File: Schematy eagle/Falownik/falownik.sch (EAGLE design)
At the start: 43 parts, among them IC1 A1382UA, IC2 A1382UA, IC3 A1382UA, IC4 A1382UA, IC5 A1382UA, IC6 A1382UA, IC7 A1382UA, IC8 A1382UA, IC9 A1382UA, Q1 VN88AF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

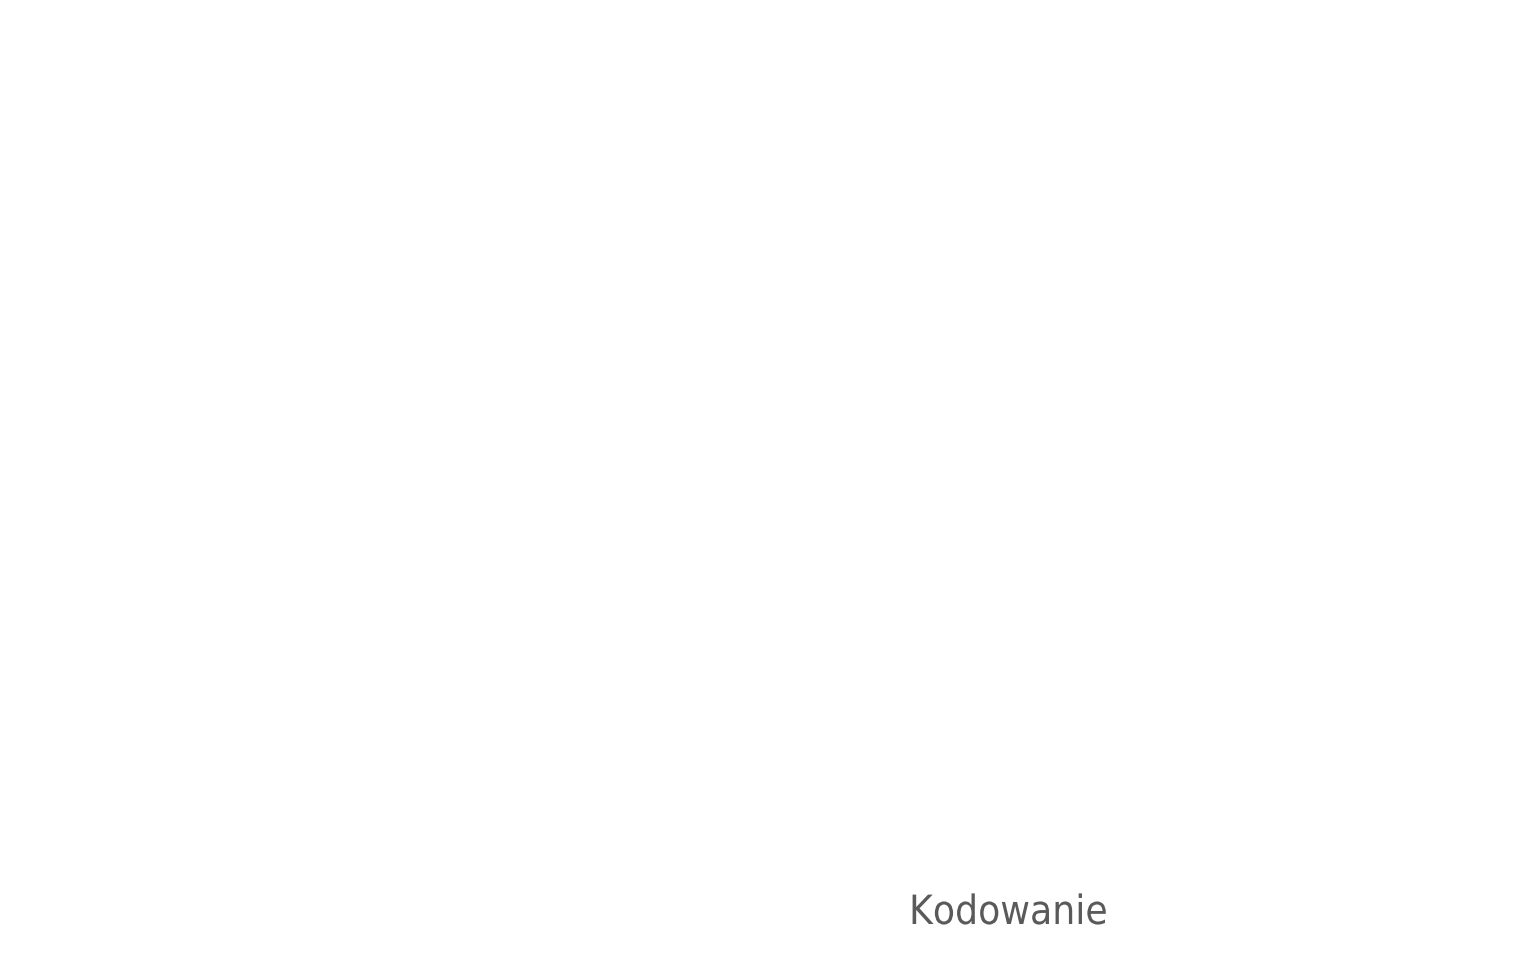
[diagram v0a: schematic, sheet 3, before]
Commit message: Dodanie kodowania
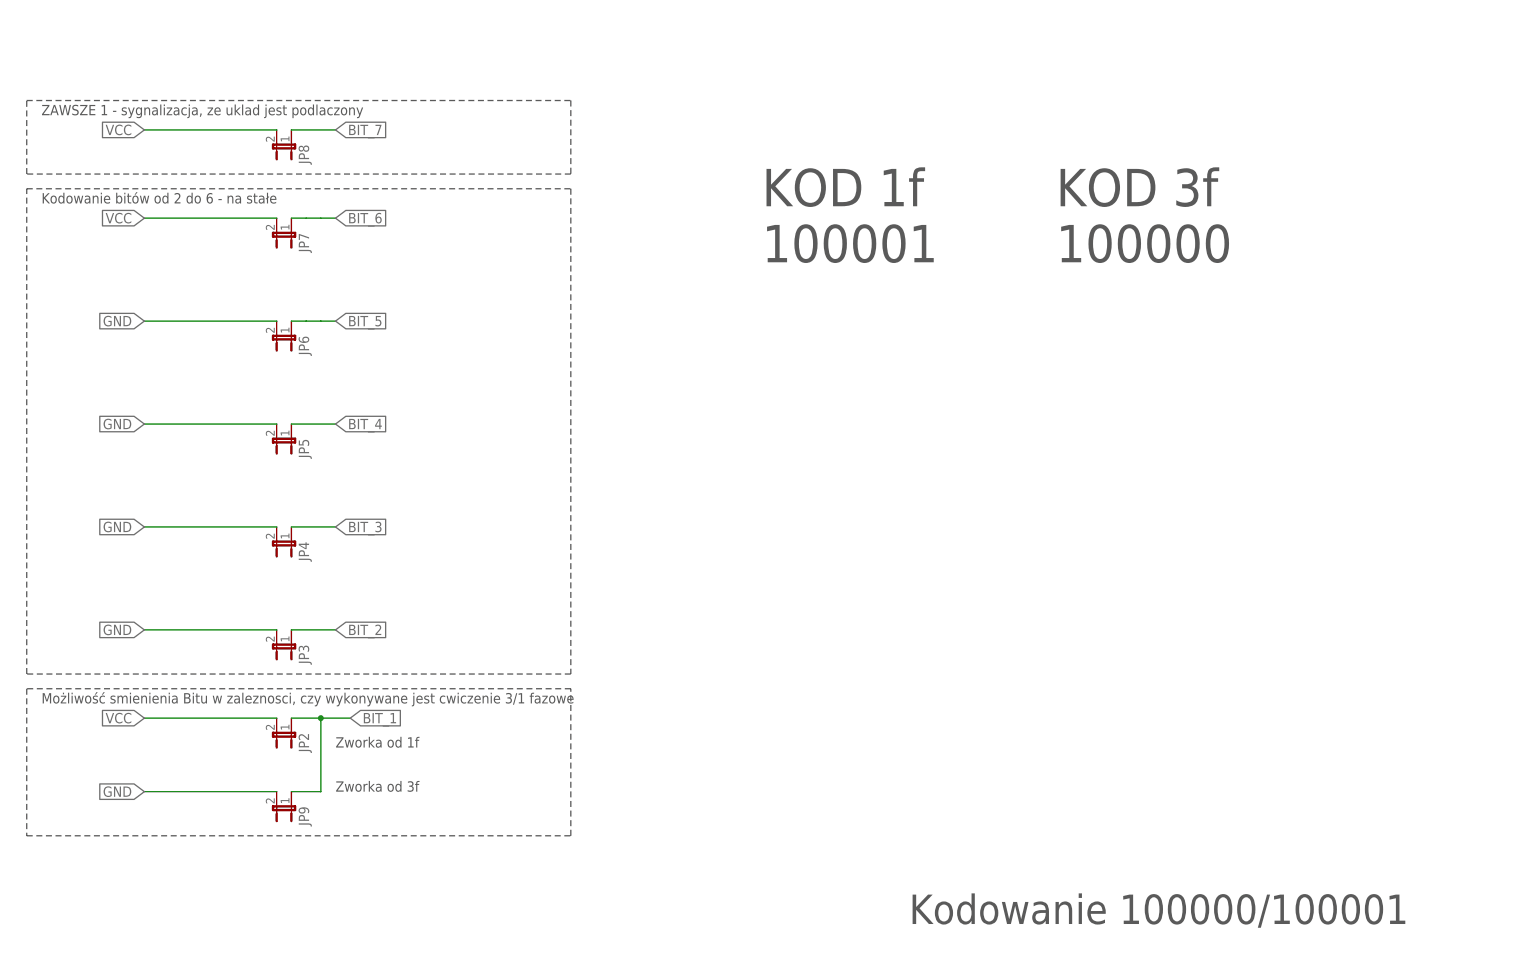
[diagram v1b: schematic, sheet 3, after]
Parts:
- added JP2, JP3, JP4, JP5, JP6, JP7, JP8, JP9: (no value), jumper:JP1E
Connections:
- net BIT_1: now also JP2.1, JP9.1
- net BIT_2: now also JP3.1
- net BIT_3: now also JP4.1
- net BIT_4: now also JP5.1
- net BIT_5: now also JP6.1
- net BIT_6: now also JP7.1
- net BIT_7: now also JP8.1
- net GND: now also JP3.2, JP4.2, JP5.2, JP6.2, JP9.2
- net VCC: now also JP2.2, JP7.2, JP8.2
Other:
- note added: "KOD 1f 100001"
- note added: "KOD 3f 100000"
- note added: "Kodowanie 100000/100001"
- note added: "Kodowanie bitów od 2 do 6 - na stałe"
- note added: "Możliwość smienienia Bitu w zaleznosci, czy wykonywane jest cwiczenie 3/1 fazowe"
- note added: "ZAWSZE 1 - sygnalizacja, ze uklad jest podlaczony"
- note added: "Zworka od 1f"
- note added: "Zworka od 3f"

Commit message: Update
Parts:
- removed Q6: VN88AF, transistor-fet:VN88AF
- added Q7: IRFP240, transistor-power:IRFP240
- Q1, Q2, Q3, Q4, Q5: value VN88AF -> IRFP240; device transistor-fet:VN88AF -> transistor-power:IRFP240
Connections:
- net GND: now also Q1.S, Q3.S, Q5.S; no longer Q2.S, Q4.S, Q6.S
- net K11: now also Q7.G; no longer Q1.G
- net K12: now also Q2.G; no longer Q3.G
- net K13: now also Q4.G; no longer Q5.G
- net K21: now also Q1.G; no longer Q2.G
- net K22: now also Q3.G; no longer Q4.G
- net K23: now also Q5.G; no longer Q6.G
- net N$1: now also Q7.D; no longer Q1.D
- net N$12: now also Q2.D; no longer Q3.D
- net N$14: now also Q3.D; no longer Q4.D
- net N$15: now also Q2.S; no longer Q3.S
- net N$23: now also Q4.D; no longer Q5.D
- net N$25: now also Q5.D; no longer Q6.D
- net N$26: now also Q4.S; no longer Q5.S
- net N$3: now also Q1.D; no longer Q2.D
- net N$4: now also Q7.S; no longer Q1.S
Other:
- note added: "Bezpiecznik 1A"
- note added: "Zmiana zadania - ćw. 1/3f"
- note removed: "Możliwość smienienia Bitu w zaleznosci, czy wykonywane jest cwiczenie 3/1 fazowe"
- moved on the sheet: JP2, JP3, JP4, JP5, JP6, JP7, JP8, JP9
